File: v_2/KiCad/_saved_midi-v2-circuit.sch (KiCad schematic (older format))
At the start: 42 parts, among them CON1 IDC-14, CON2 AVR-ISP-10, CON3 IDC-14, J1 Screw_Terminal_01x12, J2 Conn_01x04, J3 DIN-8, J4 Conn_01x17, J6 USB_B, J7 to_midi_adapter_USB, J8 to_midi_adapter_MIDI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

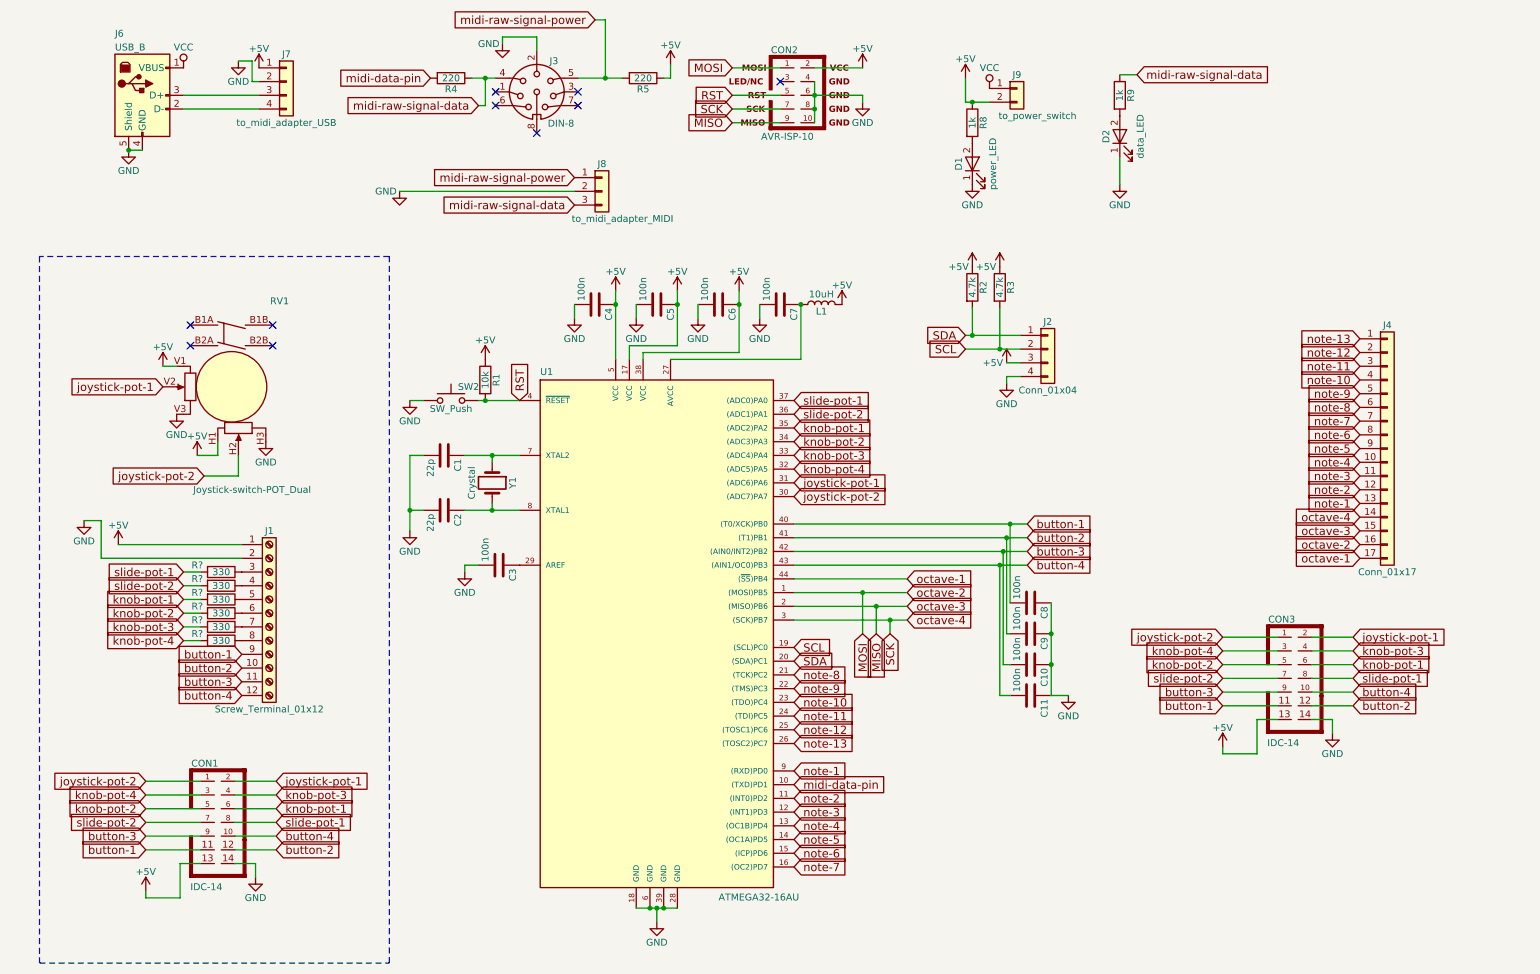
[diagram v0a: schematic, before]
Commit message: adc first success
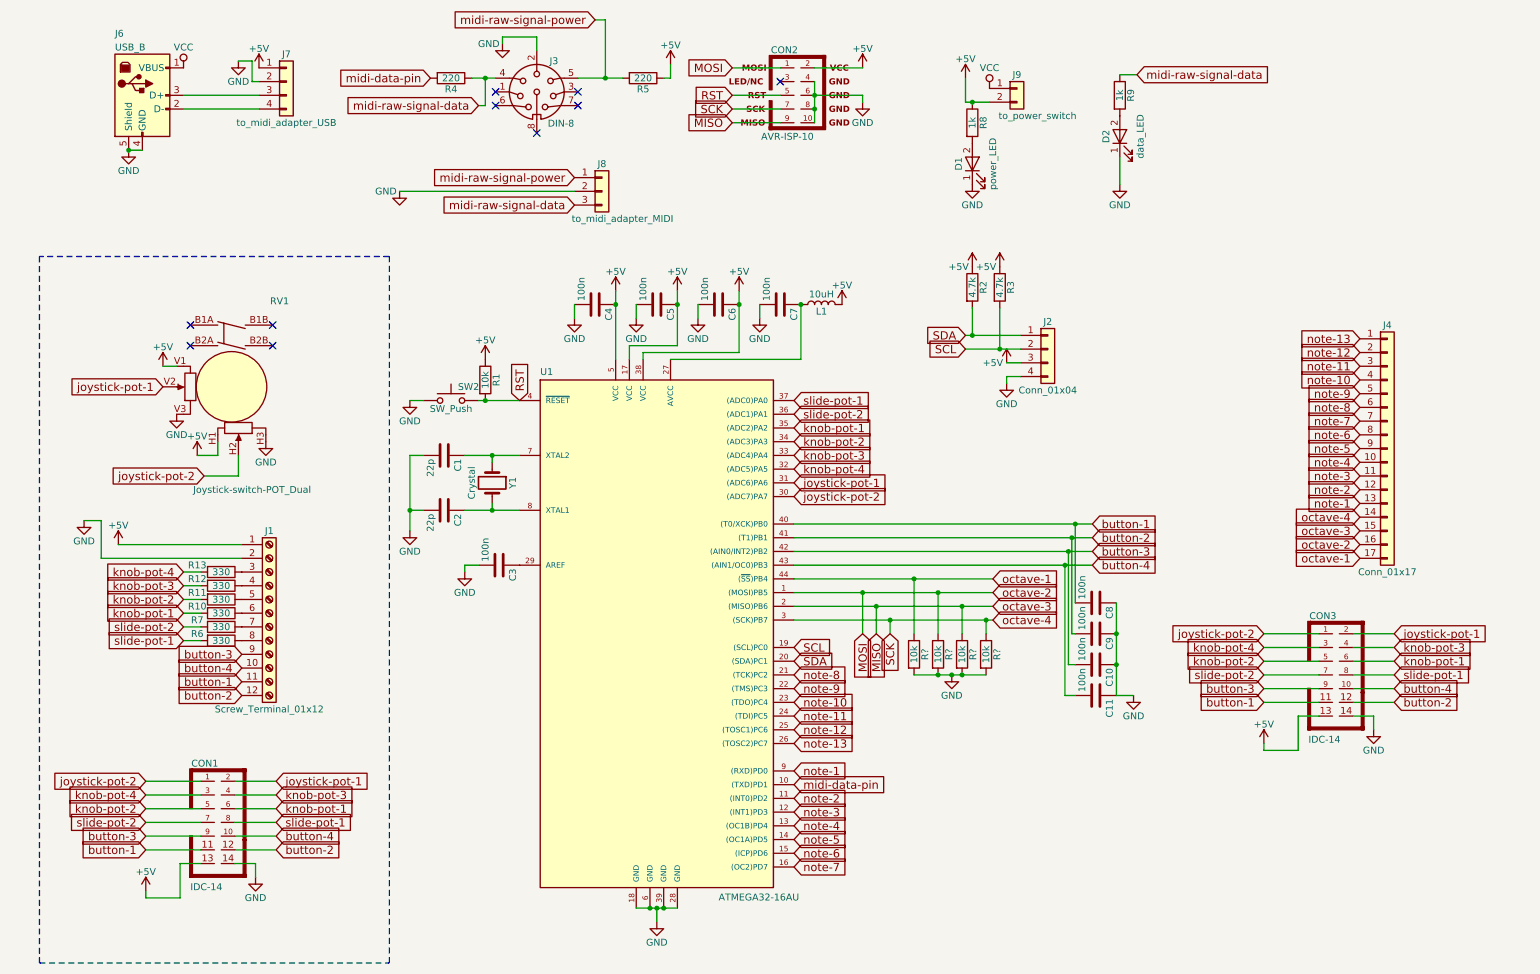
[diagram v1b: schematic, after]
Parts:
- added R? (x4): 10k, symbol R
- L1: footprint Inductors_SMD:L_1812_HandSoldering -> Inductors_SMD:L_0805_HandSoldering
- R10, R11, R12, R13, R6, R7: renamed from R?; footprint (none) -> Resistors_SMD:R_0805_HandSoldering
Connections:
- net GND: now also R?.2, R?.2, R?.2, R?.2
- net MISO: now also R?.1
- net MOSI: now also R?.1
- net SCK: now also R?.1
- net button-1: now also J1.11 (Pin_11); no longer J1.9 (Pin_9)
- net button-2: now also J1.12 (Pin_12); no longer J1.10 (Pin_10)
- net button-3: now also J1.9 (Pin_9); no longer J1.11 (Pin_11)
- net button-4: now also J1.10 (Pin_10); no longer J1.12 (Pin_12)
- net octave-1: now also R?.1
- net at J1.3 (Pin_3): now also R13.1; no longer R6.1
- net at J1.4 (Pin_4): now also R12.1; no longer R7.1
- net at J1.5 (Pin_5): now also R11.1; no longer R10.1
- net at J1.6 (Pin_6): now also R10.1; no longer R11.1
- net at J1.7 (Pin_7): now also R7.1; no longer R12.1
- net at J1.8 (Pin_8): now also R6.1; no longer R13.1
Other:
- moved on the sheet: C10, C11, C8, C9, CON3, R10, R11, R12, R13, R6, R7
